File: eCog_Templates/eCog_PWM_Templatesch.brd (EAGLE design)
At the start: 47.5 x 28 mm, 11 parts

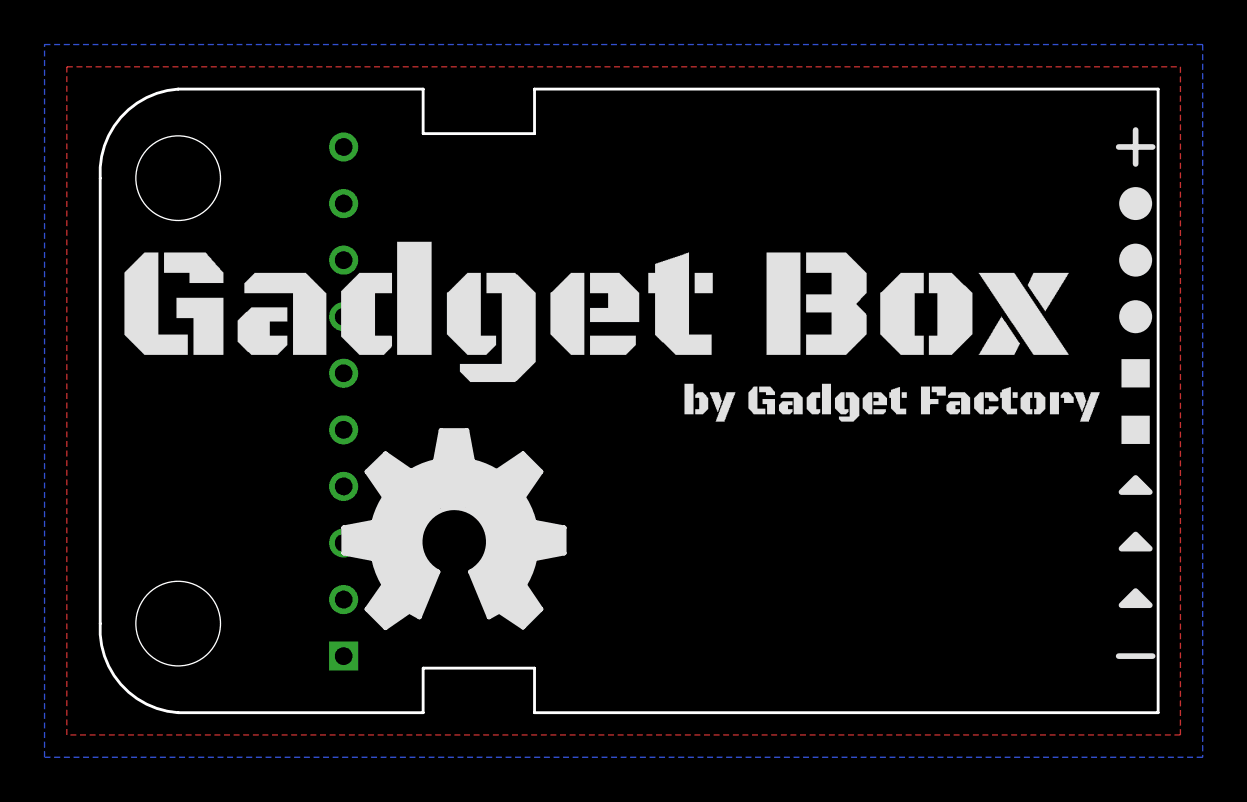
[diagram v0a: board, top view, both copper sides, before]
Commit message: Change to through hole and give bette descriptions.
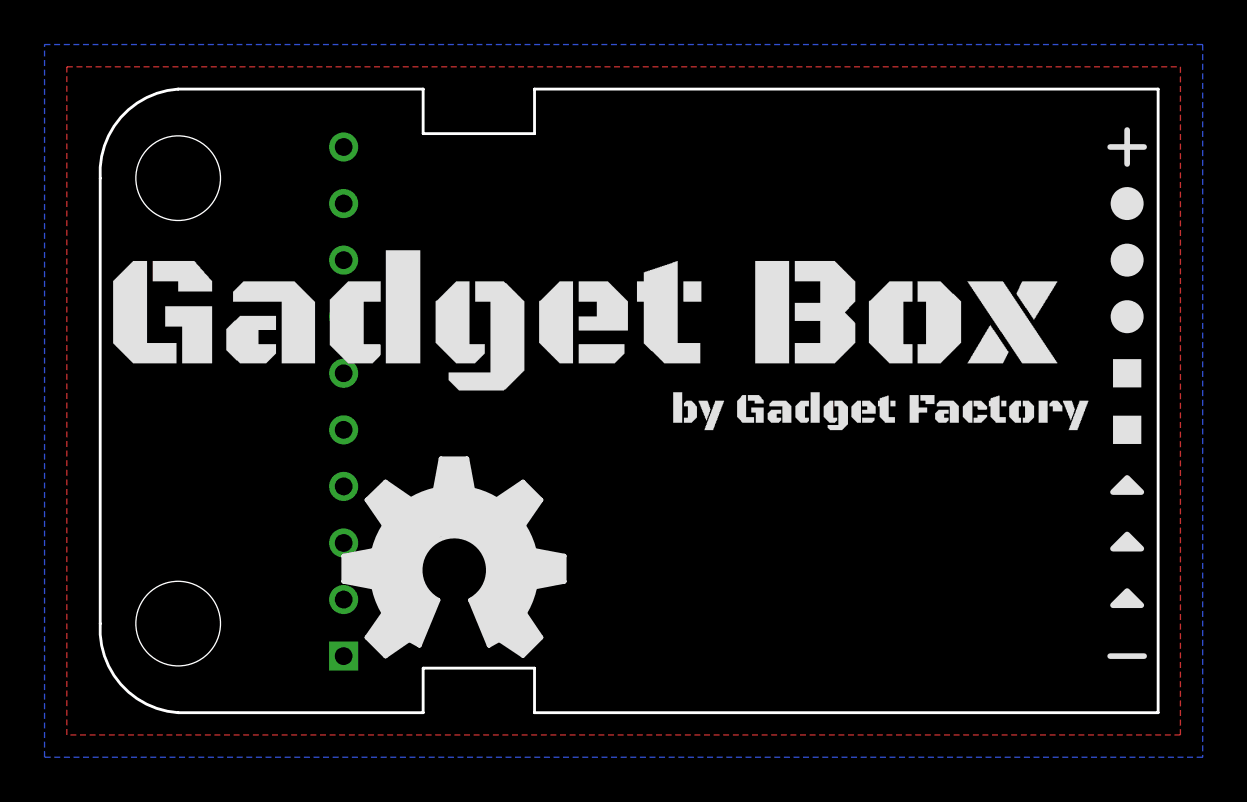
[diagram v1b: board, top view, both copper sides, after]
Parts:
- U$1: device eCogs:LEGEND_DIO -> GadgetFactory:GADGETBOX_TEXT
- U$4: device GadgetFactory:GADGETBOX_TEXT -> eCogs:LEGEND_DIO
- moved U$1 24.6 mm to (22.4, 17.4)
- moved U$4 23.7 mm to (46.6, 17.8)
- moved U$10 1.27 mm to (11.4, 2.54)
- moved U$2 0.38 mm to (46.6, 22.9)
- moved U$3 0.38 mm to (46.6, 20.3)
- moved U$5 0.38 mm to (46.6, 15.2)
- moved U$6 0.38 mm to (46.6, 12.7)
- moved U$7 0.38 mm to (46.6, 10.2)
- moved U$8 0.38 mm to (46.6, 7.62)
- moved U$9 0.38 mm to (46.6, 5.08)
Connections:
- net A2 renamed PWM3
- net A3 renamed PWM2
- removed net A1: ECOG.G0
- new net PWM1: ECOG.G3
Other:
- board text added: "0"
- board text added: "1"
- board text added: "2"
- board text added: "3"
- board text added: "4"
- board text added: "5"
- board text added: "6"
- board text added: "7"
- board text removed: "G0<>"
- board text removed: "G1<>"
- board text removed: "G2<>"
- board text removed: "G3<>"
- board text removed: "G4<>"
- board text removed: "G5<>"
- board text removed: "G6<>"
- board text removed: "G7<>"
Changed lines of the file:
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@@
 <text x="39.702" y="3.429" size="1.016" layer="22" font="vector" rot="MR0">Project Name</text>
 <text x="39.702" y="4.699" size="1.016" layer="22" font="vector" rot="MR0">eCogs</text>
-<text x="16.605" y="8.128" size="1.016" layer="22" font="vector" rot="MR180">G1&lt;&gt;</text>
-<text x="16.605" y="10.668" size="1.016" layer="22" font="vector" rot="MR180">G2&lt;&gt;</text>
-<text x="16.605" y="13.208" size="1.016" layer="22" font="vector" rot="MR180">G3&lt;&gt;</text>
-<text x="16.605" y="15.748" size="1.016" layer="22" font="vector" rot="MR180">G4&lt;&gt;</text>
-<text x="16.605" y="18.288" size="1.016" layer="22" font="vector" rot="MR180">G5&lt;&gt;</text>
-<text x="16.605" y="20.828" size="1.016" layer="22" font="vector" rot="MR180">G6&lt;&gt;</text>
-<text x="16.605" y="23.368" size="1.016" layer="22" font="vector" rot="MR180">G7&lt;&gt;</text>
-<text x="16.605" y="5.588" size="1.016" layer="22" font="vector" rot="MR180">G0&lt;&gt;</text>
+<text x="15.335" y="8.128" size="1.016" layer="22" font="vector" rot="MR180">1</text>
+<text x="15.335" y="10.668" size="1.016" layer="22" font="vector" rot="MR180">2</text>
+<text x="15.335" y="13.208" size="1.016" layer="22" font="vector" rot="MR180">3</text>
+<text x="15.335" y="15.748" size="1.016" layer="22" font="vector" rot="MR180">4</text>
+<text x="15.335" y="18.288" size="1.016" layer="22" font="vector" rot="MR180">5</text>
+<text x="15.335" y="20.828" size="1.016" layer="22" font="vector" rot="MR180">6</text>
+<text x="15.335" y="23.368" size="1.016" layer="22" font="vector" rot="MR180">7</text>
+<text x="15.335" y="5.588" size="1.016" layer="22" font="vector" rot="MR180">0</text>
 <text x="33.782" y="17.526" size="0.6096" layer="22" font="vector" rot="MR0">Copyright 2016</text>
 <text x="35.512" y="16.637" size="0.6096" layer="22" font="vector" rot="MR0">Gadget Factory, LLC</text>
-<text x="16.605" y="25.908" size="1.016" layer="22" font="vector" rot="MR180">3.3V</text>
-<text x="16.605" y="3.048" size="1.016" layer="22" font="vector" rot="MR180">GND</text>
-<wire x1="46.99" y1="26.162" x2="46.99" y2="24.638" width="0.254" layer="21"/>
-<wire x1="46.228" y1="25.4" x2="47.752" y2="25.4" width="0.254" layer="21"/>
-<wire x1="46.228" y1="2.54" x2="47.752" y2="2.54" width="0.254" layer="21"/>
+<text x="15.335" y="25.908" size="1.016" layer="22" font="vector" rot="MR180">3.3V</text>
+<text x="15.335" y="3.048" size="1.016" layer="22" font="vector" rot="MR180">GND</text>
+<wire x1="45.847" y1="25.4" x2="47.371" y2="25.4" width="0.254" layer="21"/>
+<wire x1="46.609" y1="26.162" x2="46.609" y2="24.638" width="0.254" layer="21"/>
+<wire x1="45.847" y1="2.54" x2="47.371" y2="2.54" width="0.254" layer="21"/>
 </plain>
 <attributes>
@@
 <elements>
 <element name="ECOG" library="eCogs" package="ECOG_GENERAL_TH" value="ECOG_GENERAL_ROWTHROUGHOLE" x="0" y="0" smashed="yes"/>
-<element name="U$2" library="eCogs" package="LEGEND_DIO" value="" x="46.99" y="22.86"/>
-<element name="U$3" library="eCogs" package="LEGEND_DIO" value="" x="46.99" y="20.32"/>
-<element name="U$5" library="eCogs" package="LEGEND_PWM" value="" x="46.99" y="15.24"/>
-<element name="U$6" library="eCogs" package="LEGEND_PWM" value="" x="46.99" y="12.7"/>
-<element name="U$7" library="eCogs" package="LEGEND_ANALOG" value="" x="46.99" y="10.16"/>
-<element name="U$8" library="eCogs" package="LEGEND_ANALOG" value="" x="46.99" y="7.62"/>
-<element name="U$9" library="eCogs" package="LEGEND_ANALOG" value="" x="46.99" y="5.08"/>
-<element name="U$1" library="eCogs" package="LEGEND_DIO" value="" x="46.99" y="17.78"/>
-<element name="U$4" library="GadgetFactory" package="GADGETBOX_TEXT" value="" x="22.86" y="17.78"/>
-<element name="U$10" library="ohw-logo" package="OSHW_FILLX350_NOTEXT" value="" x="11.43" y="3.81"/>
+<element name="U$2" library="eCogs" package="LEGEND_DIO" value="" x="46.609" y="22.86"/>
+<element name="U$3" library="eCogs" package="LEGEND_DIO" value="" x="46.609" y="20.32"/>
+<element name="U$5" library="eCogs" package="LEGEND_PWM" value="" x="46.609" y="15.24"/>
+<element name="U$6" library="eCogs" package="LEGEND_PWM" value="" x="46.609" y="12.7"/>
+<element name="U$7" library="eCogs" package="LEGEND_ANALOG" value="" x="46.609" y="10.16"/>
+<element name="U$8" library="eCogs" package="LEGEND_ANALOG" value="" x="46.609" y="7.62"/>
+<element name="U$9" library="eCogs" package="LEGEND_ANALOG" value="" x="46.609" y="5.08"/>
+<element name="U$1" library="GadgetFactory" package="GADGETBOX_TEXT" value="" x="22.352" y="17.399"/>
+<element name="U$10" library="ohw-logo" package="OSHW_FILLX350_NOTEXT" value="" x="11.43" y="2.54"/>
+<element name="U$4" library="eCogs" package="LEGEND_DIO" value="" x="46.609" y="17.78"/>
 </elements>
 <signals>
@@
 </polygon>
 </signal>
-<signal name="A1">
-<contactref element="ECOG" pad="G0"/>
-</signal>
-<signal name="A2">
+<signal name="PWM1">
+<contactref element="ECOG" pad="G3"/>
+</signal>
+<signal name="PWM2">
+<contactref element="ECOG" pad="G2"/>
+</signal>
+<signal name="PWM3">
 <contactref element="ECOG" pad="G1"/>
 </signal>
-<signal name="A3">
-<contactref element="ECOG" pad="G2"/>
-</signal>
 </signals>
